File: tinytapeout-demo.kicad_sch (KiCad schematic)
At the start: 125 parts, among them J1 Conn_01x06, J12 613012243121, J13 613012243121, J14 613012243121, J15 USB4500-03-0-A_REVA, J16 2x20_P2.54mm_Pinheader, J17 Conn_01x03, J18 2x20_P2.54mm_Pinheader, J2 Conn_01x04, J3 613012243121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

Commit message: v1.0.4 alpha as assembled for test run
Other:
- note added: "TinyTapeout 4/5 Demo Board"
- note added: "https://github.com/TinyTapeout/tt-demo-pcb"
- note removed: "TinyTapeout 4/5 Demo Board (preliminary)"
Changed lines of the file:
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@@
     (effects (font (size 1.27 1.27)) (justify left bottom))
   )
-  (text "TinyTapeout 4/5 Demo Board (preliminary)" (at 168.91 17.78 0)
+  (text "TinyTapeout 4/5 Demo Board" (at 168.91 17.78 0)
     (effects (font (size 4 4) (thickness 0.4) bold) (justify left bottom))
   )
@@
     (effects (font (size 1 1)) (justify right bottom))
   )
+  (text "https://github.com/TinyTapeout/tt-demo-pcb" (at 355.6 76.2 0)
+    (effects (font (size 1.27 1.27)) (justify left bottom) (href "https://github.com/TinyTapeout/tt-demo-pcb"))
+  )
   (text "TX" (at 219.075 147.32 90)

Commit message: v1.0.5, post alpha pcba modifications
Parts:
- added C44, C45, C46, C47: C_33p_0402_50V, Capacitor_SMD:C_0402_1005Metric, symbol psypassives:C_33p_0402_50V
- added C48, C49: 1uF, Capacitor_SMD:C_0603_1608Metric, symbol Device:C_Small
- added D5, D6: TVS, Resistor_SMD:R_0603_1608Metric, symbol Device:D_TVS
- added FB1: FerriteBead_Small, Inductor_SMD:L_0603_1608Metric, symbol Device:FerriteBead_Small
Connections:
- net +5V: now also C49.1, FB1.2; no longer F1.2
- net CC1: now also C46.1
- net CC2: now also C47.1
- net GND: now also C44.2, C45.2, C46.2, C47.2, C48.2, C49.2, D5.1 (A1), D6.1 (A1)
- net usb_d+: now also C45.1, D6.2 (A2)
- net usb_d-: now also C44.1, D5.2 (A2)
- new net vfused: C48.1, F1.2, FB1.1
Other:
- title: TinyTapeout 4/5 Demo Board PRELIM -> TinyTapeout 4/5 Demo Board
- moved on the sheet: C3, F1, J15, R16, R20, R21

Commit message: minor cleanup/comments
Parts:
- FB1: value FerriteBead_Small -> 120R
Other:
- note added: "Options for basic filtering and ESD on USB conn. At a min, populate the ferrite and TVS diodes."
- note added: "TVS diodes"
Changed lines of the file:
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@@
     (effects (font (size 1 1)) (justify left bottom))
   )
+  (text "Options for basic filtering \nand ESD on USB conn.\nAt a min, populate the ferrite \nand TVS diodes."
+    (at 116.84 86.36 0)
+    (effects (font (size 1.27 1.27)) (justify left bottom))
+  )
   (text "Note: All this decoupling should be amply handled by the carrier.  \nWould rather DNP than regret."
     (at 270.51 88.9 0)
@@
     (effects (font (size 2 2)) (justify right bottom))
   )
-  (text "90R Diff" (at 131.445 59.69 0)
+  (text "90R Diff" (at 132.08 62.23 0)
     (effects (font (size 1.27 1.27)) (justify left bottom))
   )
@@
     (effects (font (size 1.27 1.27) (color 0 194 194 1)) (justify left bottom))
   )
+  (text "TVS diodes" (at 160.02 86.36 0)
+    (effects (font (size 1.27 1.27)) (justify left bottom))
+  )
   (text "sck" (at 243.84 139.954 90)
     (effects (font (size 1 1) (color 255 113 0 1)) (justify left bottom))
@@
       (effects (font (size 1.27 1.27)) hide)
     )
+    (property "Variant" "" (at 60.96 111.76 0)
+      (effects (font (size 1.27 1.27)) hide)
+    )
     (pin "1")
     (pin "2")
@@
   (symbol (lib_id "Device:C_Small") (at 157.48 35.56 0) (unit 1)
     (in_bom yes) (on_board yes) (dnp no)
-    (property "Reference" "C48" (at 152.4 34.29 0)
+    (property "Reference" "C48" (at 153.67 34.29 0)
       (effects (font (size 1 1)) (justify left))
     )
-    (property "Value" "1uF" (at 152.4 36.83 0)
+    (property "Value" "1uF" (at 153.67 36.83 0)
       (effects (font (size 1 1)) (justify left))
     )
@@
   (symbol (lib_id "Device:C_Small") (at 166.37 35.56 0) (unit 1)
     (in_bom yes) (on_board yes) (dnp no)
-    (property "Reference" "C49" (at 168.6941 34.5714 0)
+    (property "Reference" "C49" (at 167.64 34.29 0)
       (effects (font (size 1 1)) (justify left))
     )
-    (property "Value" "1uF" (at 168.6941 36.5611 0)
+    (property "Value" "1uF" (at 167.64 36.83 0)
       (effects (font (size 1 1)) (justify left))
     )
@@
   )
   (symbol (lib_id "Device:FerriteBead_Small") (at 161.29 31.75 90) (unit 1)
-    (in_bom yes) (on_board yes) (dnp no) (fields_autoplaced)
-    (property "Reference" "FB1" (at 161.2519 28.3281 90)
+    (in_bom yes) (on_board yes) (dnp no)
+    (property "Reference" "FB1" (at 161.29 29.21 90)
       (effects (font (size 1.27 1.27)))
     )
-    (property "Value" "FerriteBead_Small" (at 161.2519 28.3281 90)
-      (effects (font (size 1.27 1.27)) hide)
+    (property "Value" "120R" (at 161.29 34.29 90)
+      (effects (font (size 1 1)))
     )
     (property "Footprint" "Inductor_SMD:L_0603_1608Metric" (at 161.29 33.528 90)

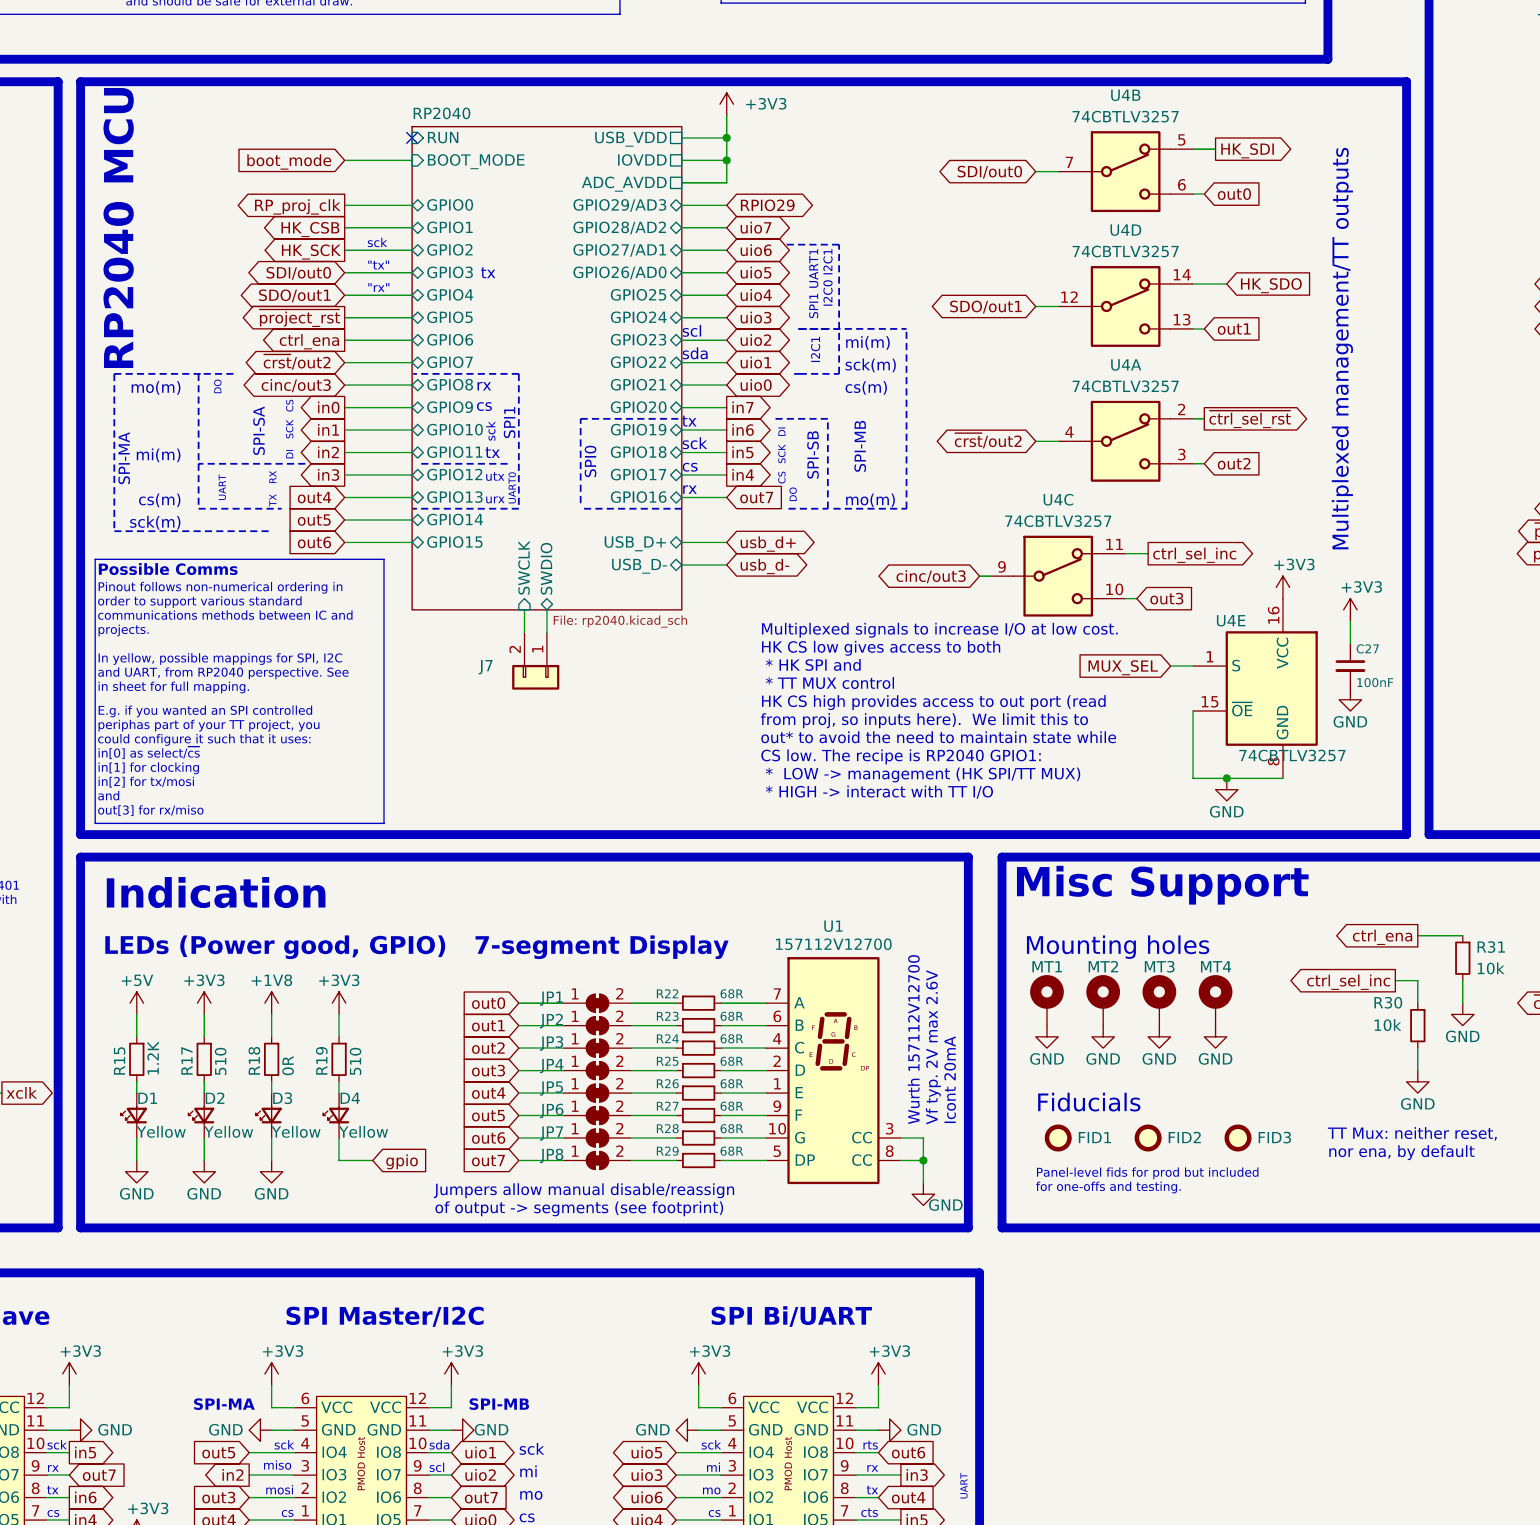
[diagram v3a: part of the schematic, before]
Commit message: remap out0/out1 and MUX, routing, silk rework
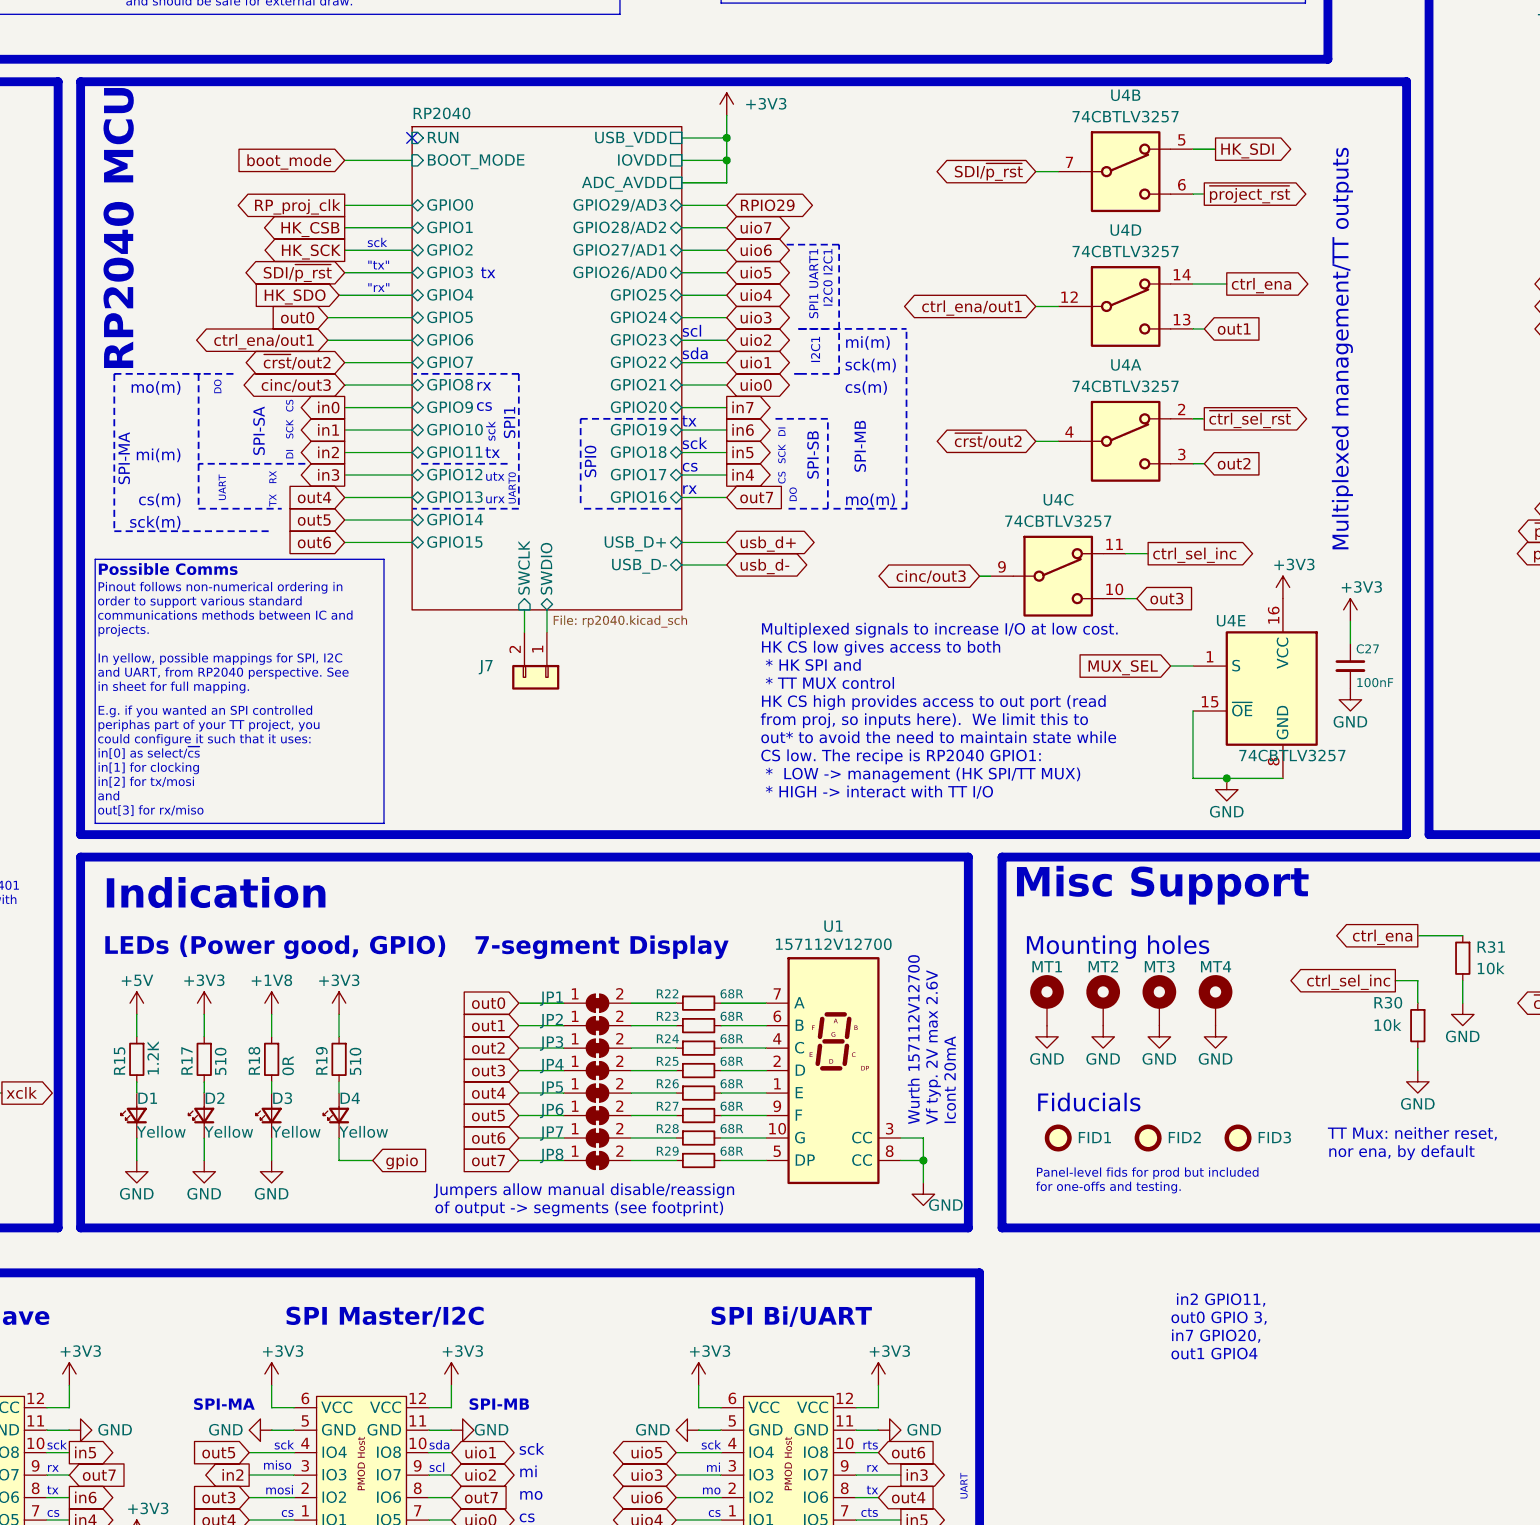
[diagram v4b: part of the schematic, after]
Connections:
- net HK_SDO: no longer U4.14
- net ctrl_ena: now also U4.14
- net out0: no longer U4.6
- net ~{project_rst}: now also U4.6
- net SDI/out0 renamed SDI/~{p_rst}
- net SDO/out1 renamed ctrl_ena/out1
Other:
- note added: "in2 GPIO11, out0 GPIO 3, in7 GPIO20, out1 GPIO4"
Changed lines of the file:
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@@
     (stroke (width 0) (type default))
   )
-  (wire (pts (xy 226.695 123.19) (xy 234.315 123.19))
+  (wire (pts (xy 226.06 123.19) (xy 234.315 123.19))
     (stroke (width 0) (type default))
   )
@@
     (stroke (width 0) (type default))
   )
-  (wire (pts (xy 226.695 128.27) (xy 234.315 128.27))
+  (wire (pts (xy 224.79 128.27) (xy 234.315 128.27))
     (stroke (width 0) (type default))
   )
@@
     (stroke (width 0) (type default))
   )
-  (wire (pts (xy 226.695 125.73) (xy 234.315 125.73))
+  (wire (pts (xy 224.79 125.73) (xy 234.315 125.73))
     (stroke (width 0) (type default))
   )
@@
     (effects (font (size 1 1) (color 255 0 255 1)) (justify right bottom))
   )
+  (text " in2 GPIO11, \nout0 GPIO 3, \nin7 GPIO20, \nout1 GPIO4"
+    (at 320.04 243.84 0)
+    (effects (font (size 1.27 1.27)) (justify left bottom))
+  )
   (text "SPI-Bi" (at 258.445 265.43 0)
     (effects (font (size 1 1) (color 255 113 0 1)) (justify left bottom))
@@
     )
   )
-  (global_label "SDO{slash}out1" (shape bidirectional) (at 304.8 124.46 180) (fields_autoplaced)
+  (global_label "ctrl_ena{slash}out1" (shape bidirectional) (at 304.8 124.46 180) (fields_autoplaced)
     (effects (font (size 1.27 1.27)) (justify right))
-    (property "Intersheetrefs" "${INTERSHEET_REFS}" (at 291.3298 124.46 0)
+    (property "Intersheetrefs" "${INTERSHEET_REFS}" (at 287.5199 124.46 0)
       (effects (font (size 1.27 1.27)) (justify right) hide)
     )
   )
+  (global_label "out1" (shape input) (at 323.85 127 0) (fields_autoplaced)
+    (effects (font (size 1.27 1.27)) (justify left))
+    (property "Intersheetrefs" "${INTERSHEET_REFS}" (at 331.0684 127 0)
+      (effects (font (size 1.27 1.27)) (justify left) hide)
+    )
+  )
   (global_label "out7" (shape input) (at 269.875 146.05 0) (fields_autoplaced)
     (effects (font (size 1.27 1.27)) (justify left))
@@
     )
   )
-  (global_label "SDI{slash}out0" (shape bidirectional) (at 226.695 120.65 180) (fields_autoplaced)
+  (global_label "SDI{slash}~{p_rst}" (shape bidirectional) (at 226.695 120.65 180) (fields_autoplaced)
     (effects (font (size 1.27 1.27)) (justify right))
-    (property "Intersheetrefs" "${INTERSHEET_REFS}" (at 213.9505 120.65 0)
+    (property "Intersheetrefs" "${INTERSHEET_REFS}" (at 213.5271 120.65 0)
       (effects (font (size 1.27 1.27)) (justify right) hide)
     )
@@
     )
   )
-  (global_label "~{project_rst}" (shape output) (at 226.695 125.73 180) (fields_autoplaced)
-    (effects (font (size 1.27 1.27)) (justify right))
-    (property "Intersheetrefs" "${INTERSHEET_REFS}" (at 213.6103 125.73 0)
-      (effects (font (size 1.27 1.27)) (justify right) hide)
+  (global_label "~{project_rst}" (shape output) (at 323.85 111.76 0) (fields_autoplaced)
+    (effects (font (size 1.27 1.27)) (justify left))
+    (property "Intersheetrefs" "${INTERSHEET_REFS}" (at 336.9347 111.76 0)
+      (effects (font (size 1.27 1.27)) (justify left) hide)
     )
   )
@@
     )
   )
-  (global_label "ctrl_ena" (shape output) (at 226.695 128.27 180) (fields_autoplaced)
-    (effects (font (size 1.27 1.27)) (justify right))
-    (property "Intersheetrefs" "${INTERSHEET_REFS}" (at 216.0899 128.27 0)
-      (effects (font (size 1.27 1.27)) (justify right) hide)
+  (global_label "ctrl_ena" (shape output) (at 326.39 121.92 0) (fields_autoplaced)
+    (effects (font (size 1.27 1.27)) (justify left))
+    (property "Intersheetrefs" "${INTERSHEET_REFS}" (at 336.9951 121.92 0)
+      (effects (font (size 1.27 1.27)) (justify left) hide)
     )
   )
@@
     )
   )
-  (global_label "HK_SDO" (shape input) (at 326.39 121.92 0) (fields_autoplaced)
-    (effects (font (size 1.27 1.27)) (justify left))
-    (property "Intersheetrefs" "${INTERSHEET_REFS}" (at 336.7533 121.92 0)
-      (effects (font (size 1.27 1.27)) (justify left) hide)
+  (global_label "HK_SDO" (shape input) (at 226.06 123.19 180) (fields_autoplaced)
+    (effects (font (size 1.27 1.27)) (justify right))
+    (property "Intersheetrefs" "${INTERSHEET_REFS}" (at 215.6967 123.19 0)
+      (effects (font (size 1.27 1.27)) (justify right) hide)
     )
   )
@@
     )
   )
-  (global_label "SDI{slash}out0" (shape bidirectional) (at 304.8 109.22 180) (fields_autoplaced)
+  (global_label "SDI{slash}~{p_rst}" (shape bidirectional) (at 304.8 109.22 180) (fields_autoplaced)
     (effects (font (size 1.27 1.27)) (justify right))
-    (property "Intersheetrefs" "${INTERSHEET_REFS}" (at 292.0555 109.22 0)
+    (property "Intersheetrefs" "${INTERSHEET_REFS}" (at 291.6321 109.22 0)
       (effects (font (size 1.27 1.27)) (justify right) hide)
     )
@@
     )
   )
-  (global_label "SDO{slash}out1" (shape bidirectional) (at 226.695 123.19 180) (fields_autoplaced)
-    (effects (font (size 1.27 1.27)) (justify right))
-    (property "Intersheetrefs" "${INTERSHEET_REFS}" (at 213.2248 123.19 0)
-      (effects (font (size 1.27 1.27)) (justify right) hide)
-    )
-  )
   (global_label "in3" (shape output) (at 68.58 60.96 0) (fields_autoplaced)
     (effects (font (size 1.27 1.27)) (justify left))
@@
     )
   )
-  (global_label "out0" (shape input) (at 323.85 111.76 0) (fields_autoplaced)
-    (effects (font (size 1.27 1.27)) (justify left))
-    (property "Intersheetrefs" "${INTERSHEET_REFS}" (at 331.0684 111.76 0)
-      (effects (font (size 1.27 1.27)) (justify left) hide)
+  (global_label "out0" (shape input) (at 224.79 125.73 180) (fields_autoplaced)
+    (effects (font (size 1.27 1.27)) (justify right))
+    (property "Intersheetrefs" "${INTERSHEET_REFS}" (at 217.5716 125.73 0)
+      (effects (font (size 1.27 1.27)) (justify right) hide)
     )
   )
@@
     )
   )
-  (global_label "out1" (shape input) (at 323.85 127 0) (fields_autoplaced)
-    (effects (font (size 1.27 1.27)) (justify left))
-    (property "Intersheetrefs" "${INTERSHEET_REFS}" (at 331.0684 127 0)
-      (effects (font (size 1.27 1.27)) (justify left) hide)
+  (global_label "ctrl_ena{slash}out1" (shape bidirectional) (at 224.79 128.27 180) (fields_autoplaced)
+    (effects (font (size 1.27 1.27)) (justify right))
+    (property "Intersheetrefs" "${INTERSHEET_REFS}" (at 207.5099 128.27 0)
+      (effects (font (size 1.27 1.27)) (justify right) hide)
     )
   )
